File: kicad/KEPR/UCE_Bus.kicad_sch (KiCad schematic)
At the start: 1 part, among them J11 10141995-005RLF

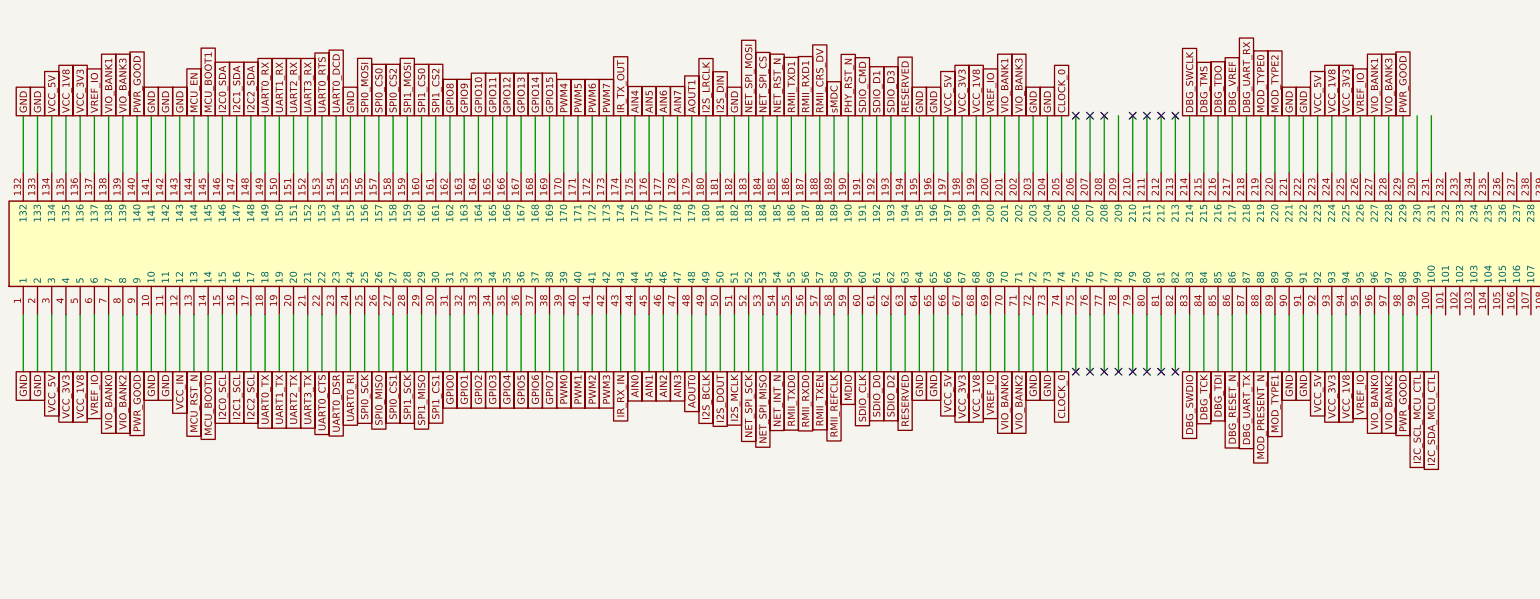
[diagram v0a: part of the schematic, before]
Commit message: Adicionado o display oled e mais trilhas.
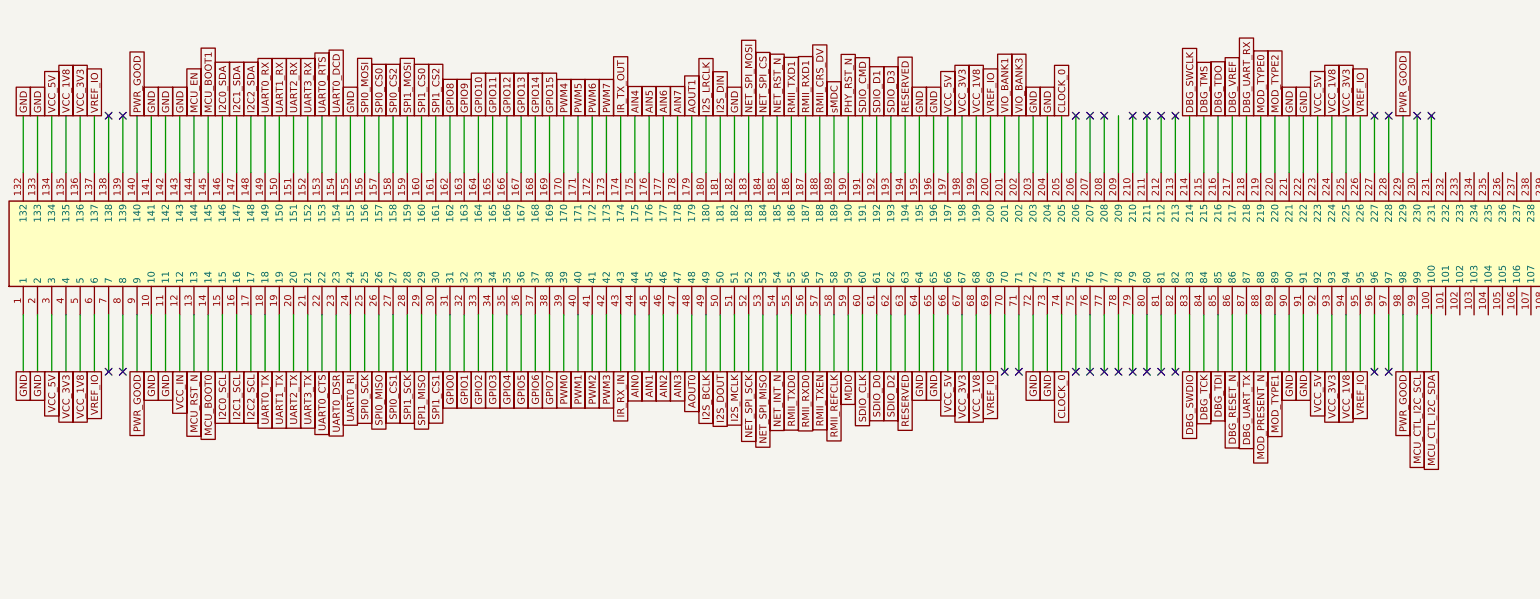
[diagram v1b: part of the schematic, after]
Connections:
- net VIO_BANK1: no longer J11.138, J11.227
- net VIO_BANK3: no longer J11.139, J11.228
- net I2C_SCL_MCU_CTL renamed MCU_CTL_I2C_SCL
- net I2C_SDA_MCU_CTL renamed MCU_CTL_I2C_SDA
- removed net VIO_BANK0: J11.7, J11.70, J11.96
- removed net VIO_BANK2: J11.71, J11.8, J11.97
- no-connect marks 15 -> 27
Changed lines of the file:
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@@
 	)
 	(no_connect
+		(at 60.96 83.82)
+	)
+	(no_connect
+		(at 289.56 83.82)
+	)
+	(no_connect
+		(at 289.56 38.1)
+	)
+	(no_connect
 		(at 243.84 83.82)
 	)
@@
 	)
 	(no_connect
+		(at 297.18 38.1)
+	)
+	(no_connect
+		(at 63.5 83.82)
+	)
+	(no_connect
+		(at 220.98 83.82)
+	)
+	(no_connect
 		(at 251.46 83.82)
 	)
 	(no_connect
+		(at 60.96 38.1)
+	)
+	(no_connect
+		(at 287.02 38.1)
+	)
+	(no_connect
 		(at 251.46 38.1)
 	)
@@
 	)
 	(no_connect
+		(at 63.5 38.1)
+	)
+	(no_connect
+		(at 223.52 83.82)
+	)
+	(no_connect
+		(at 287.02 83.82)
+	)
+	(no_connect
 		(at 248.92 83.82)
 	)
@@
 	)
 	(no_connect
+		(at 294.64 38.1)
+	)
+	(no_connect
 		(at 246.38 38.1)
 	)
@@
 		)
 	)
-	(global_label "VIO_BANK2"
-		(shape passive)
-		(at 223.52 83.82 270)
-		(effects
-			(font
-				(size 1.27 1.27)
-			)
-			(justify right bottom)
-		)
-		(property "Intersheetrefs" "${INTERSHEET_REFS}"
-			(at 223.52 83.82 90)
-			(effects
-				(font
-					(size 1.27 1.27)
-				)
-				(justify left)
-				(hide yes)
-			)
-		)
-	)
 	(global_label "UART0_RX"
 		(shape passive)
@@
 		)
 	)
-	(global_label "VIO_BANK0"
-		(shape passive)
-		(at 220.98 83.82 270)
-		(effects
-			(font
-				(size 1.27 1.27)
-			)
-			(justify right bottom)
-		)
-		(property "Intersheetrefs" "${INTERSHEET_REFS}"
-			(at 220.98 83.82 90)
-			(effects
-				(font
-					(size 1.27 1.27)
-				)
-				(hide yes)
-			)
-		)
-	)
 	(global_label "VREF_IO"
 		(shape passive)
@@
 		)
 	)
-	(global_label "VIO_BANK2"
-		(shape passive)
-		(at 63.5 83.82 270)
-		(effects
-			(font
-				(size 1.27 1.27)
-			)
-			(justify right bottom)
-		)
-		(property "Intersheetrefs" "${INTERSHEET_REFS}"
-			(at 63.5 83.82 90)
-			(effects
-				(font
-					(size 1.27 1.27)
-				)
-				(justify left)
-				(hide yes)
-			)
-		)
-	)
 	(global_label "SPI0_CS1"
 		(shape passive)
@@
 		)
 	)
-	(global_label "VIO_BANK0"
-		(shape passive)
-		(at 60.96 83.82 270)
-		(effects
-			(font
-				(size 1.27 1.27)
-			)
-			(justify right bottom)
-		)
-		(property "Intersheetrefs" "${INTERSHEET_REFS}"
-			(at 60.96 83.82 90)
-			(effects
-				(font
-					(size 1.27 1.27)
-				)
-				(justify left)
-				(hide yes)
-			)
-		)
-	)
 	(global_label "GND"
 		(shape passive)
@@
 		)
 	)
-	(global_label "VIO_BANK3"
-		(shape passive)
-		(at 289.56 38.1 90)
-		(effects
-			(font
-				(size 1.27 1.27)
-			)
-			(justify left bottom)
-		)
-		(property "Intersheetrefs" "${INTERSHEET_REFS}"
-			(at 289.56 38.1 90)
-			(effects
-				(font
-					(size 1.27 1.27)
-				)
-				(justify left)
-				(hide yes)
-			)
-		)
-	)
 	(global_label "AOUT1"
 		(shape passive)
@@
 		)
 	)
-	(global_label "VIO_BANK3"
-		(shape passive)
-		(at 63.5 38.1 90)
-		(effects
-			(font
-				(size 1.27 1.27)
-			)
-			(justify left bottom)
-		)
-		(property "Intersheetrefs" "${INTERSHEET_REFS}"
-			(at 63.5 38.1 90)
-			(effects
-				(font
-					(size 1.27 1.27)
-				)
-				(justify left)
-				(hide yes)
-			)
-		)
-	)
-	(global_label "VIO_BANK1"
-		(shape passive)
-		(at 287.02 38.1 90)
-		(effects
-			(font
-				(size 1.27 1.27)
-			)
-			(justify left bottom)
-		)
-		(property "Intersheetrefs" "${INTERSHEET_REFS}"
-			(at 287.02 38.1 90)
-			(effects
-				(font
-					(size 1.27 1.27)
-				)
-				(justify left)
-				(hide yes)
-			)
-		)
-	)
 	(global_label "I2C0_SCL"
 		(shape passive)
@@
 		)
 	)
-	(global_label "I2C_SDA_MCU_CTL"
+	(global_label "MCU_CTL_I2C_SDA"
 		(shape passive)
 		(at 297.18 83.82 270)
@@
 		)
 	)
-	(global_label "I2C_SCL_MCU_CTL"
+	(global_label "MCU_CTL_I2C_SCL"
 		(shape passive)
 		(at 294.64 83.82 270)
@@
 		)
 	)
-	(global_label "VIO_BANK1"
-		(shape passive)
-		(at 60.96 38.1 90)
-		(effects
-			(font
-				(size 1.27 1.27)
-			)
-			(justify left bottom)
-		)
-		(property "Intersheetrefs" "${INTERSHEET_REFS}"
-			(at 60.96 38.1 90)
-			(effects
-				(font
-					(size 1.27 1.27)
-				)
-				(justify left)
-				(hide yes)
-			)
-		)
-	)
 	(global_label "NET_SPI_CS"
 		(shape passive)
@@
 		)
 	)
-	(global_label "VIO_BANK2"
-		(shape passive)
-		(at 289.56 83.82 270)
-		(effects
-			(font
-				(size 1.27 1.27)
-			)
-			(justify right bottom)
-		)
-		(property "Intersheetrefs" "${INTERSHEET_REFS}"
-			(at 289.56 83.82 90)
-			(effects
-				(font
-					(size 1.27 1.27)
-				)
-				(justify left)
-				(hide yes)
-			)
-		)
-	)
 	(global_label "RMII_TXD0"
 		(shape passive)
@@
 			(effects
 				(font
-					(size 1.27 1.27)
-				)
-				(justify left)
-				(hide yes)
-			)
-		)
-	)
-	(global_label "VIO_BANK0"
-		(shape passive)
-		(at 287.02 83.82 270)
-		(effects
-			(font
-				(size 1.27 1.27)
-			)
-			(justify right bottom)
-		)
-		(property "Intersheetrefs" "${INTERSHEET_REFS}"
-			(at 287.02 83.82 90)
-			(effects
-				(font

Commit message: mais ajustes de trilha.
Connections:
- net RESERVED: no longer names the net of J11.194
- net RESERVED: no longer J11.63
- net VIO_BANK1: no longer names the net of J11.201
- net VIO_BANK3: no longer names the net of J11.202
- no-connect marks 27 -> 87

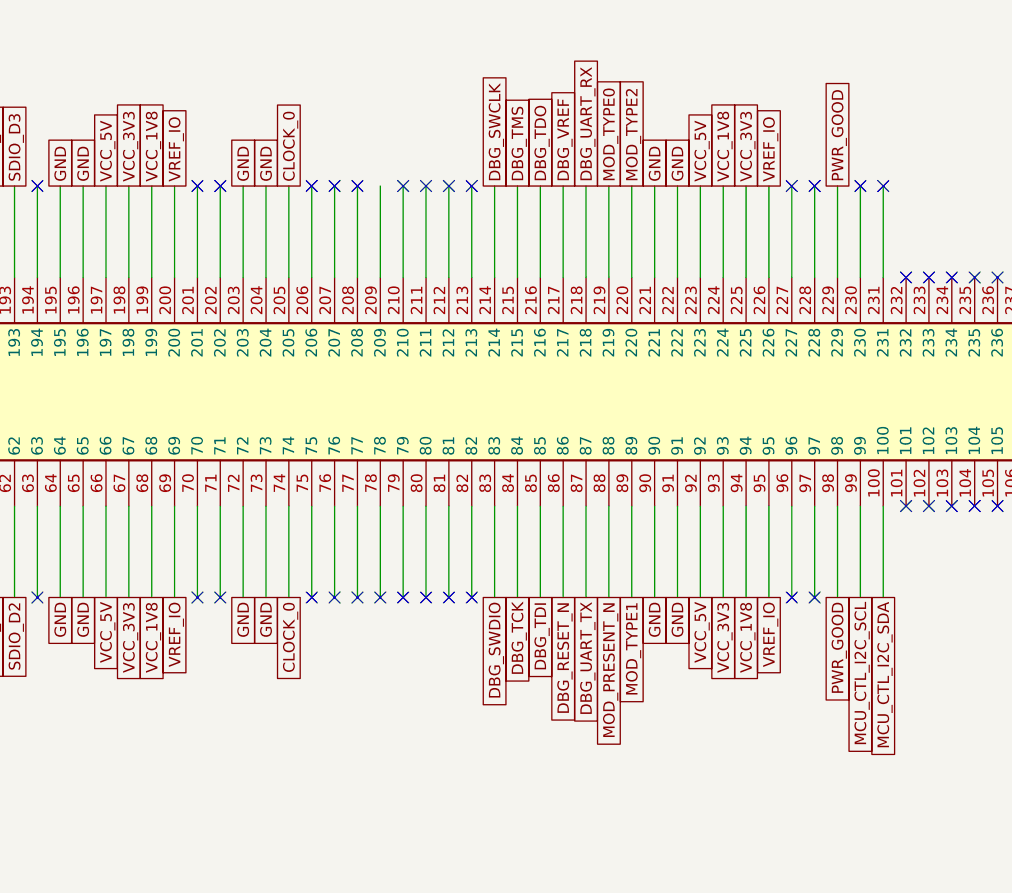
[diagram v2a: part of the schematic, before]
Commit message: Mais trilhas e vias lançadas
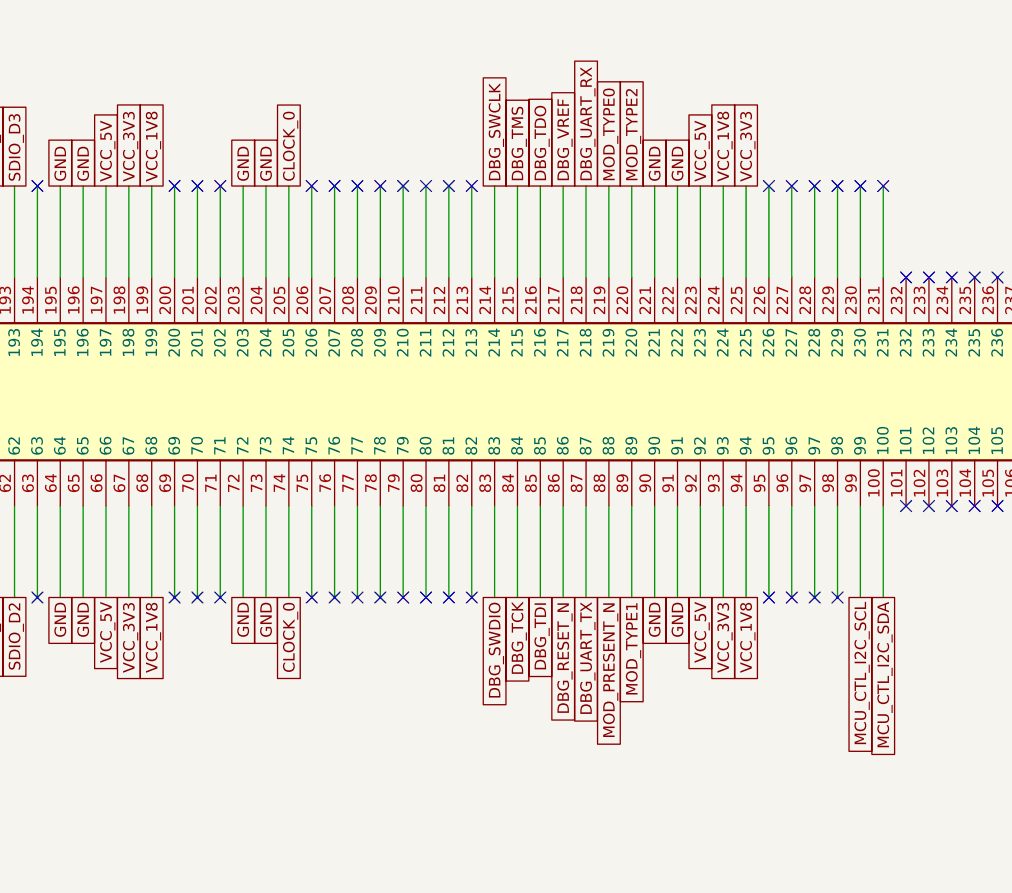
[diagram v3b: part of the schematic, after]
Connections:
- net PWR_GOOD: no longer J11.229, J11.98
- net VREF_IO: no longer J11.200, J11.226, J11.69, J11.95
- no-connect marks 87 -> 94
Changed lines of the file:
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@@
 	)
 	(no_connect
+		(at 292.1 38.1)
+	)
+	(no_connect
 		(at 347.98 73.66)
 	)
@@
 	)
 	(no_connect
+		(at 284.48 38.1)
+	)
+	(no_connect
 		(at 340.36 73.66)
 	)
@@
 	)
 	(no_connect
+		(at 284.48 83.82)
+	)
+	(no_connect
 		(at 299.72 48.26)
 	)
@@
 	)
 	(no_connect
+		(at 218.44 38.1)
+	)
+	(no_connect
 		(at 358.14 48.26)
 	)
@@
 	)
 	(no_connect
+		(at 241.3 38.1)
+	)
+	(no_connect
 		(at 233.68 38.1)
 	)
@@
 	)
 	(no_connect
+		(at 218.44 83.82)
+	)
+	(no_connect
 		(at 350.52 48.26)
 	)
@@
 	)
 	(no_connect
+		(at 292.1 83.82)
+	)
+	(no_connect
 		(at 302.26 48.26)
 	)
@@
 		)
 	)
-	(global_label "VREF_IO"
-		(shape passive)
-		(at 284.48 38.1 90)
-		(effects
-			(font
-				(size 1.27 1.27)
-			)
-			(justify left bottom)
-		)
-		(property "Intersheetrefs" "${INTERSHEET_REFS}"
-			(at 284.48 38.1 90)
-			(effects
-				(font
-					(size 1.27 1.27)
-				)
-				(hide yes)
-			)
-		)
-	)
 	(global_label "AIN4"
 		(shape passive)
@@
 		)
 	)
-	(global_label "VREF_IO"
-		(shape passive)
-		(at 218.44 38.1 90)
-		(effects
-			(font
-				(size 1.27 1.27)
-			)
-			(justify left bottom)
-		)
-		(property "Intersheetrefs" "${INTERSHEET_REFS}"
-			(at 218.44 38.1 90)
-			(effects
-				(font
-					(size 1.27 1.27)
-				)
-				(hide yes)
-			)
-		)
-	)
 	(global_label "UART0_RTS"
 		(shape passive)
@@
 		)
 	)
-	(global_label "PWR_GOOD"
-		(shape passive)
-		(at 292.1 38.1 90)
-		(effects
-			(font
-				(size 1.27 1.27)
-			)
-			(justify left bottom)
-		)
-		(property "Intersheetrefs" "${INTERSHEET_REFS}"
-			(at 292.1 38.1 90)
-			(effects
-				(font
-					(size 1.27 1.27)
-				)
-				(justify left)
-				(hide yes)
-			)
-		)
-	)
 	(global_label "GPIO7"
 		(shape passive)
@@
 		)
 	)
-	(global_label "PWR_GOOD"
-		(shape passive)
-		(at 292.1 83.82 270)
-		(effects
-			(font
-				(size 1.27 1.27)
-			)
-			(justify right bottom)
-		)
-		(property "Intersheetrefs" "${INTERSHEET_REFS}"
-			(at 292.1 83.82 90)
-			(effects
-				(font
-					(size 1.27 1.27)
-				)
-				(justify right)
-				(hide yes)
-			)
-		)
-	)
 	(global_label "MCU_BOOT1"
 		(shape passive)
@@
 		)
 	)
-	(global_label "VREF_IO"
-		(shape passive)
-		(at 284.48 83.82 270)
-		(effects
-			(font
-				(size 1.27 1.27)
-			)
-			(justify right bottom)
-		)
-		(property "Intersheetrefs" "${INTERSHEET_REFS}"
-			(at 284.48 83.82 90)
-			(effects
-				(font
-					(size 1.27 1.27)
-				)
-				(justify left)
-				(hide yes)
-			)
-		)
-	)
 	(global_label "RMII_TXEN"
 		(shape passive)
@@
 				(hide yes)
 			)
-		)
-	)
-	(global_label "VREF_IO"
-		(shape passive)
-		(at 218.44 83.82 270)
-		(effects
-			(font
-				(size 1.27 1.27)
-			)
-			(justify right bottom)
-		)
-		(property "Intersheetrefs" "${INTERSHEET_REFS}"
-			(at 218.44 83.82 90)
-			(effects
-				(font
-					(size 1.27 1.27)
-				)
-				(hide yes)
-			)
